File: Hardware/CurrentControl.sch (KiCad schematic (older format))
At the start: 24 parts, among them J4 Screw_Terminal_01x03, Q1 BUK7M45-40EX, SW1 SW_SPST, U3 MCP14A0302, U4 MCP6L02x-xMS

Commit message: Replaced gate driver with opamp. Replaced feedback circuit with unity gain buffer
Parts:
- removed D1: LED_Small_ALT, Capacitor_SMD:C_0805_2012Metric_Pad1.15x1.40mm_HandSolder, symbol Device:LED_Small_ALT
- removed D2: BAT54W, Package_TO_SOT_SMD:SOT-323_SC-70, symbol Diode:BAT54W
- removed R3: 1K, Resistor_SMD:R_0603_1608Metric_Pad1.05x0.95mm_HandSolder, symbol Device:R_Small
- removed SW1: SW_SPST, Button_Switch_THT:SW_CuK_OS102011MA1QN1_SPDT_Angled, symbol Switch:SW_SPST
- removed U3: MCP14A0302, Package_SO:SOIC-8_3.9x4.9mm_P1.27mm, symbol E-Load-rescue:MCP14A0302-E-Load
- removed unit 2 of U4
- added R22: 2.7k, Resistor_SMD:R_0603_1608Metric_Pad1.05x0.95mm_HandSolder, symbol Device:R_Small
- added R23: 15, Resistor_SMD:R_0603_1608Metric_Pad1.05x0.95mm_HandSolder, symbol Device:R_Small
- added U3: ADA4898-2, Package_SO:SOIC-8-1EP_3.9x4.9mm_P1.27mm_EP2.41x3.81mm, symbol Amplifier_Operational:ADA4898-2
- C15: value 1u -> 100nF
- R20: value 4.32k -> 10.2k
- R21: value 10.2k -> 1k
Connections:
- wire segments 70 -> 67
- no-connect marks 0 -> 1

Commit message: Changed the PWM control circuit
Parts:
- removed U3: ADA4898-2, Package_SO:SOIC-8-1EP_3.9x4.9mm_P1.27mm_EP2.41x3.81mm, symbol Amplifier_Operational:ADA4898-2
- removed U4: MCP6L02x-xMS, Package_SO:MSOP-8_3x3mm_P0.65mm, symbol Amplifier_Operational:MCP6L02x-xMS
- added C16, C17: 1n, Capacitor_SMD:C_0603_1608Metric_Pad1.05x0.95mm_HandSolder, symbol Device:C_Small
- added R24: 46.4k, Resistor_SMD:R_0603_1608Metric_Pad1.05x0.95mm_HandSolder, symbol Device:R_Small
- added R25: 50, Resistor_SMD:R_0603_1608Metric_Pad1.05x0.95mm_HandSolder, symbol Device:R_Small
- added R26: 20k, Resistor_SMD:R_0603_1608Metric_Pad1.05x0.95mm_HandSolder, symbol Device:R_Small
- added R27: 10k, Resistor_SMD:R_0603_1608Metric_Pad1.05x0.95mm_HandSolder, symbol Device:R_Small
- added U3, U4, U5: TLV172IDCK, Package_TO_SOT_SMD:SOT-353_SC-70-5, symbol Amplifier_Operational:TLV172IDCK
- C13: value 0.01uF -> 1n
- C14: value 0.082uF -> 470p
- C15: value 100nF -> 1n
- R20: value 10.2k -> 25.5k
- R21: value 1k -> 21k
- R22: value 2.7k -> 23.2k
- R23: value 15 -> 50
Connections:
- net labels removed: +3.3V
- wire segments 67 -> 70
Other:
- note added: "2nd order Lowpass Butterworth filter \nG = 3 V/V\nfc = 10kHz"
- moved on the sheet: C13, C14, R23

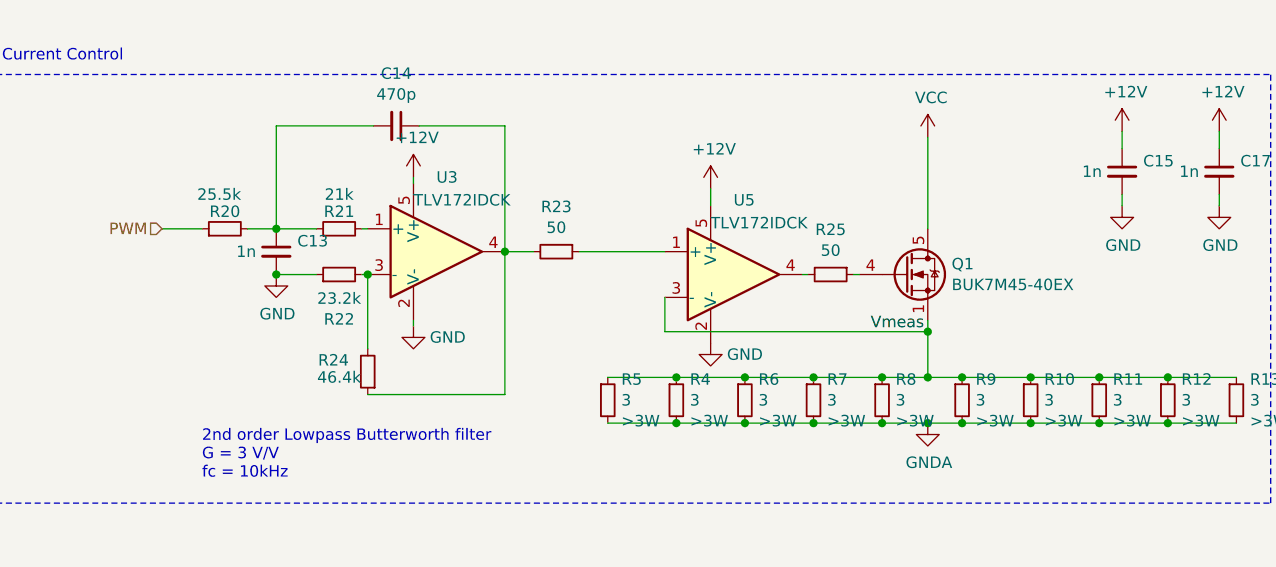
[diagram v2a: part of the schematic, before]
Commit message: Added Test points
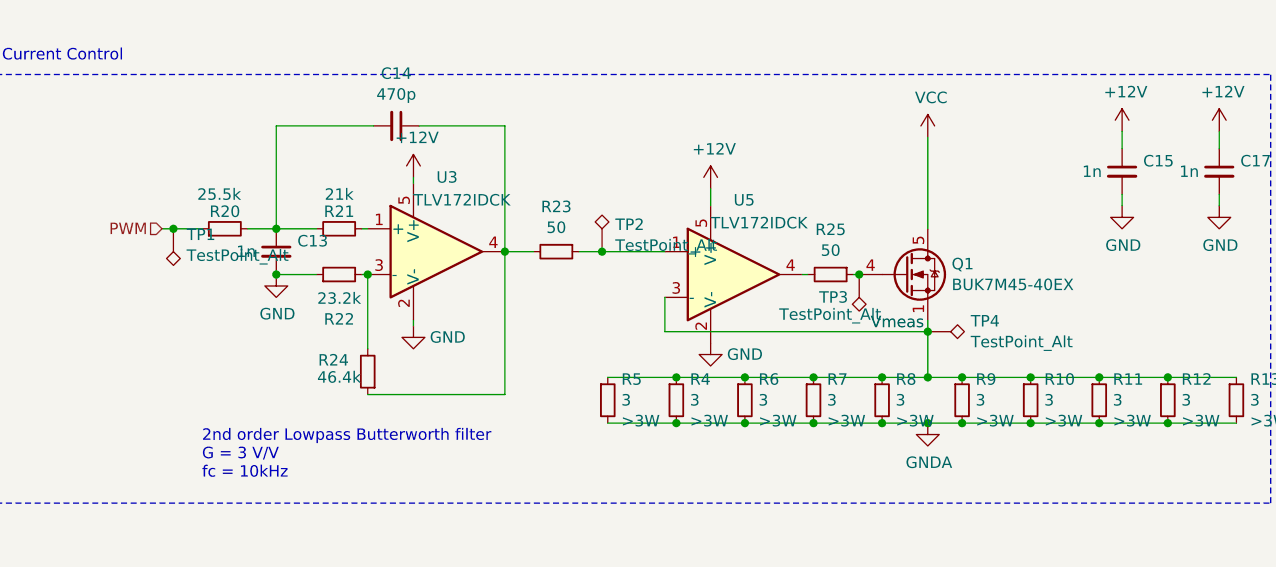
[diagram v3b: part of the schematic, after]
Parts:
- added TP1, TP2, TP3, TP4: TestPoint_Alt, TestPoint:TestPoint_Keystone_5000-5004_Miniature, symbol Connector:TestPoint_Alt
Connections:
- net PWM: now also TP1.1
- net Vmeas: now also TP4.1
- net at Q1.4 (G), R25.1: now also TP3.1
- net at R23.1, U5.1 (+): now also TP2.1
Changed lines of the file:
@@
 $EndComp
 Wire Wire Line
-	1325 3100 1500 3100
+	1325 3100 1375 3100
 Wire Wire Line
 	2200 3100 2225 3100
@@
 $EndComp
 Wire Wire Line
-	3150 3200 3525 3200
+	3150 3200 3250 3200
 $Comp
 L Device:R_Small R25
@@
 Wire Wire Line
 	9700 3750 9700 3825
+$Comp
+L Connector:TestPoint_Alt TP2
+U 1 1 5F922816
+P 3250 3200
+F 0 "TP2" H 3308 3318 50  0000 L CNN
+F 1 "TestPoint_Alt" H 3308 3227 50  0000 L CNN
+F 2 "TestPoint:TestPoint_Keystone_5000-5004_Miniature" H 3450 3200 50  0001 C CNN
+F 3 "~" H 3450 3200 50  0001 C CNN
+	1    3250 3200
+	1    0    0    -1
+$EndComp
+Connection ~ 3250 3200
+Wire Wire Line
+	3250 3200 3525 3200
+$Comp
+L Connector:TestPoint_Alt TP1
+U 1 1 5F9235DF
+P 1375 3100
+F 0 "TP1" H 1317 3126 50  0000 R CNN
+F 1 "TestPoint_Alt" H 1317 3217 50  0000 R CNN
+F 2 "TestPoint:TestPoint_Keystone_5000-5004_Miniature" H 1575 3100 50  0001 C CNN
+F 3 "~" H 1575 3100 50  0001 C CNN
+	1    1375 3100
+	-1   0    0    1
+$EndComp
+Connection ~ 1375 3100
+Wire Wire Line
+	1375 3100 1500 3100
+$Comp
+L Connector:TestPoint_Alt TP4
+U 1 1 5F924D2A
+P 4675 3550
+F 0 "TP4" V 4629 3738 50  0000 L CNN
+F 1 "TestPoint_Alt" V 4720 3738 50  0000 L CNN
+F 2 "TestPoint:TestPoint_Keystone_5000-5004_Miniature" H 4875 3550 50  0001 C CNN
+F 3 "~" H 4875 3550 50  0001 C CNN
+	1    4675 3550
+	0    1    1    0
+$EndComp
+$Comp
+L Connector:TestPoint_Alt TP3
+U 1 1 5F925FD4
+P 4375 3300
+F 0 "TP3" H 4550 3400 50  0000 R CNN
+F 1 "TestPoint_Alt" H 4725 3475 50  0000 R CNN
+F 2 "TestPoint:TestPoint_Keystone_5000-5004_Miniature" H 4575 3300 50  0001 C CNN
+F 3 "~" H 4575 3300 50  0001 C CNN
+	1    4375 3300
+	-1   0    0    1
+$EndComp
+Connection ~ 4375 3300
 $EndSCHEMATC

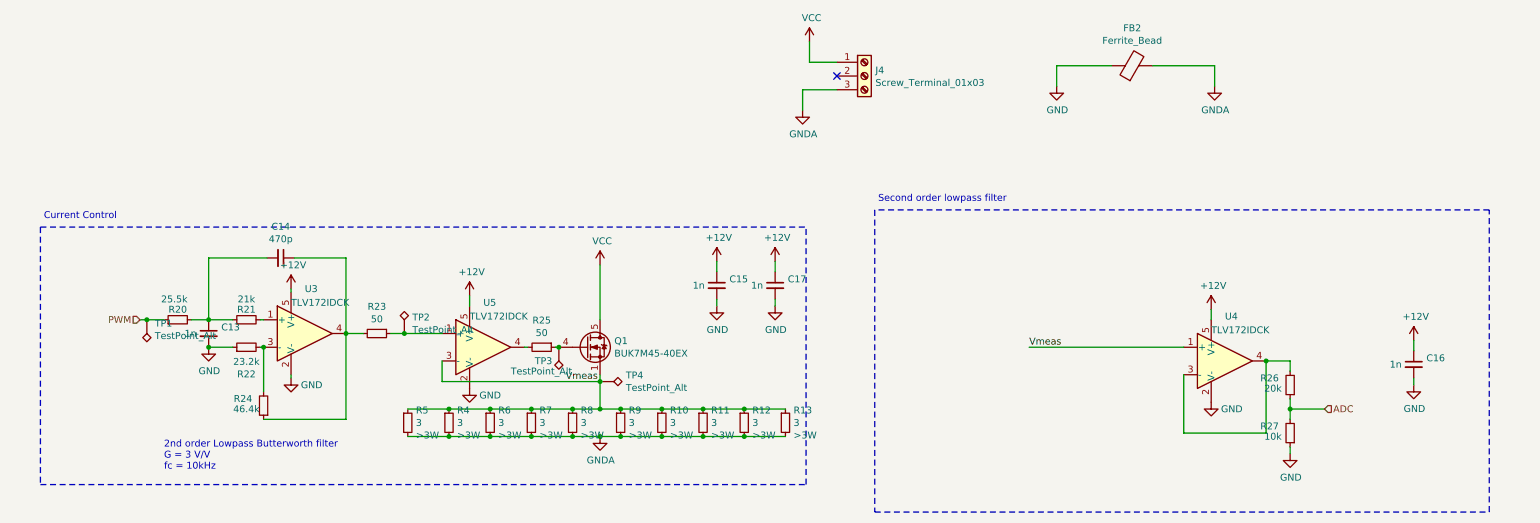
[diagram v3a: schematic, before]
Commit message: Added ADC instead of opamp. Added stiching
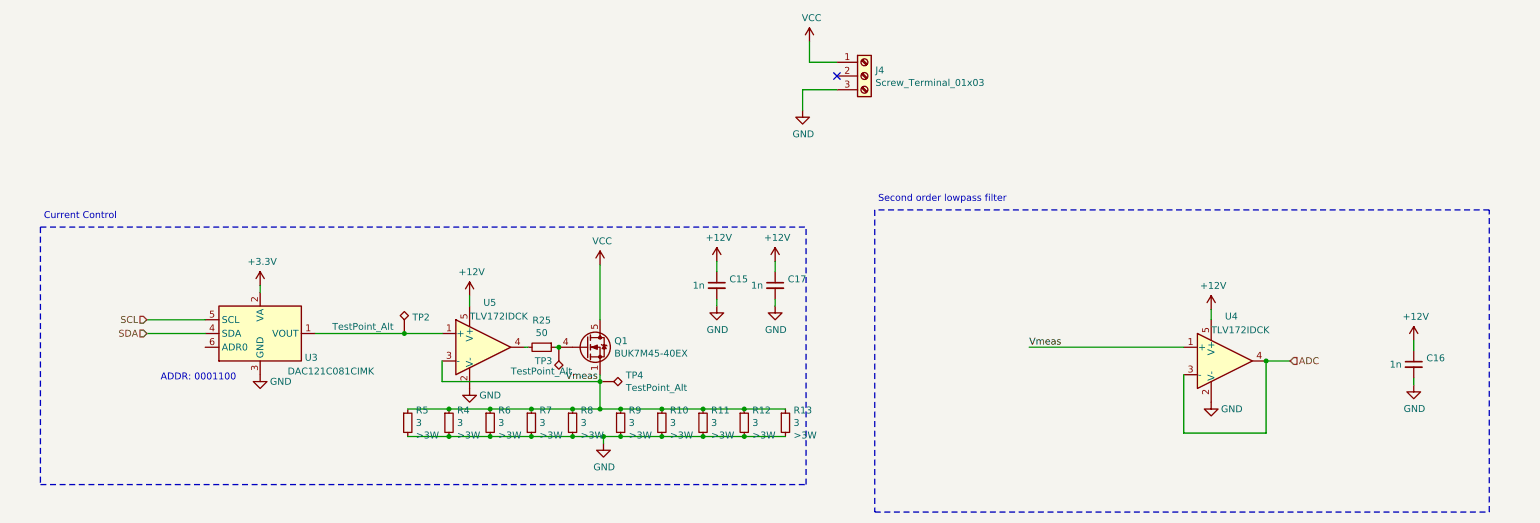
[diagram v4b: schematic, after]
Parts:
- removed C13: 1n, Capacitor_SMD:C_0603_1608Metric_Pad1.05x0.95mm_HandSolder, symbol Device:C_Small
- removed C14: 470p, Capacitor_SMD:C_0603_1608Metric_Pad1.05x0.95mm_HandSolder, symbol Device:C_Small
- removed FB2: Ferrite_Bead, Capacitor_SMD:C_1206_3216Metric, symbol Device:Ferrite_Bead
- removed R20: 25.5k, Resistor_SMD:R_0603_1608Metric_Pad1.05x0.95mm_HandSolder, symbol Device:R_Small
- removed R21: 21k, Resistor_SMD:R_0603_1608Metric_Pad1.05x0.95mm_HandSolder, symbol Device:R_Small
- removed R22: 23.2k, Resistor_SMD:R_0603_1608Metric_Pad1.05x0.95mm_HandSolder, symbol Device:R_Small
- removed R23: 50, Resistor_SMD:R_0603_1608Metric_Pad1.05x0.95mm_HandSolder, symbol Device:R_Small
- removed R24: 46.4k, Resistor_SMD:R_0603_1608Metric_Pad1.05x0.95mm_HandSolder, symbol Device:R_Small
- removed R26: 20k, Resistor_SMD:R_0603_1608Metric_Pad1.05x0.95mm_HandSolder, symbol Device:R_Small
- removed R27: 10k, Resistor_SMD:R_0603_1608Metric_Pad1.05x0.95mm_HandSolder, symbol Device:R_Small
- removed TP1: TestPoint_Alt, TestPoint:TestPoint_Keystone_5000-5004_Miniature, symbol Connector:TestPoint_Alt
- removed U3: TLV172IDCK, Package_TO_SOT_SMD:SOT-353_SC-70-5, symbol Amplifier_Operational:TLV172IDCK
- added U3: DAC121C081CIMK, Package_TO_SOT_SMD:SOT-23-6, symbol Analog_DAC:DAC121C081CIMK
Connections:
- net GNDA is gone; now on net GND: J4.3 (Pin_3), R10.2, R11.2, R12.2, R13.2, R4.2, R5.2, R6.2, R7.2, R8.2, R9.2
- net ADC: now also U4.3 (-), U4.4
- net GND: now also U3.3 (GND)
- net at TP2.1, U5.1 (+): now also U3.1 (VOUT)
- new net +3V3: U3.2 (VA)
- new net SCL: U3.5 (SCL)
- new net SDA: U3.4 (SDA)
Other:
- note added: "ADDR: 0001100"
- note removed: "2nd order Lowpass Butterworth filter \nG = 3 V/V\nfc = 10kHz"

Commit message: Minor changes
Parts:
- added R20: 1k, Resistor_SMD:R_0603_1608Metric_Pad1.05x0.95mm_HandSolder, symbol Device:R_Small
- C15, C16, C17: Voltage (none) -> >12V
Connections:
- net GND: now also R20.1
- net at TP2.1, U3.1 (VOUT), U5.1 (+): now also R20.2
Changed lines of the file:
@@
 F 2 "Capacitor_SMD:C_0603_1608Metric_Pad1.05x0.95mm_HandSolder" H 10600 3425 50  0001 C CNN
 F 3 "~" H 10600 3425 50  0001 C CNN
+F 4 ">12V" H 10750 3350 50  0000 C CNN "Voltage"
 	1    10600 3425
 	1    0    0    -1
@@
 F 2 "Capacitor_SMD:C_0603_1608Metric_Pad1.05x0.95mm_HandSolder" H 5525 2850 50  0001 C CNN
 F 3 "~" H 5525 2850 50  0001 C CNN
+F 4 ">12V" H 5625 2750 50  0000 C CNN "Voltage"
 	1    5525 2850
 	1    0    0    -1
@@
 F 2 "Capacitor_SMD:C_0603_1608Metric_Pad1.05x0.95mm_HandSolder" H 5950 2850 50  0001 C CNN
 F 3 "~" H 5950 2850 50  0001 C CNN
+F 4 ">12V" H 6075 2750 50  0000 C CNN "Voltage"
 	1    5950 2850
 	1    0    0    -1
@@
 	1    0    0    -1
 $EndComp
-Wire Wire Line
-	2600 3200 3250 3200
 $Comp
 L power:GND #PWR0125
@@
 	1    0    0    -1
 $EndComp
+$Comp
+L Device:R_Small R20
+U 1 1 5F83F1D4
+P 3250 3475
+F 0 "R20" V 3054 3475 50  0000 C CNN
+F 1 "1k" V 3145 3475 50  0000 C CNN
+F 2 "Resistor_SMD:R_0603_1608Metric_Pad1.05x0.95mm_HandSolder" H 3250 3475 50  0001 C CNN
+F 3 "~" H 3250 3475 50  0001 C CNN
+	1    3250 3475
+	-1   0    0    1
+$EndComp
+Wire Wire Line
+	2600 3200 3250 3200
+Wire Wire Line
+	3250 3200 3250 3375
+$Comp
+L power:GND #PWR01
+U 1 1 5F842985
+P 3250 3575
+F 0 "#PWR01" H 3250 3325 50  0001 C CNN
+F 1 "GND" H 3400 3525 50  0000 C CNN
+F 2 "" H 3250 3575 50  0001 C CNN
+F 3 "" H 3250 3575 50  0001 C CNN
+	1    3250 3575
+	1    0    0    -1
+$EndComp
